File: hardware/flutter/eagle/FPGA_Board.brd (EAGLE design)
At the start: 100 x 77 mm, 38 parts, among them IC1 AT45DB161D-SU, U2 XC3S50AVQ100

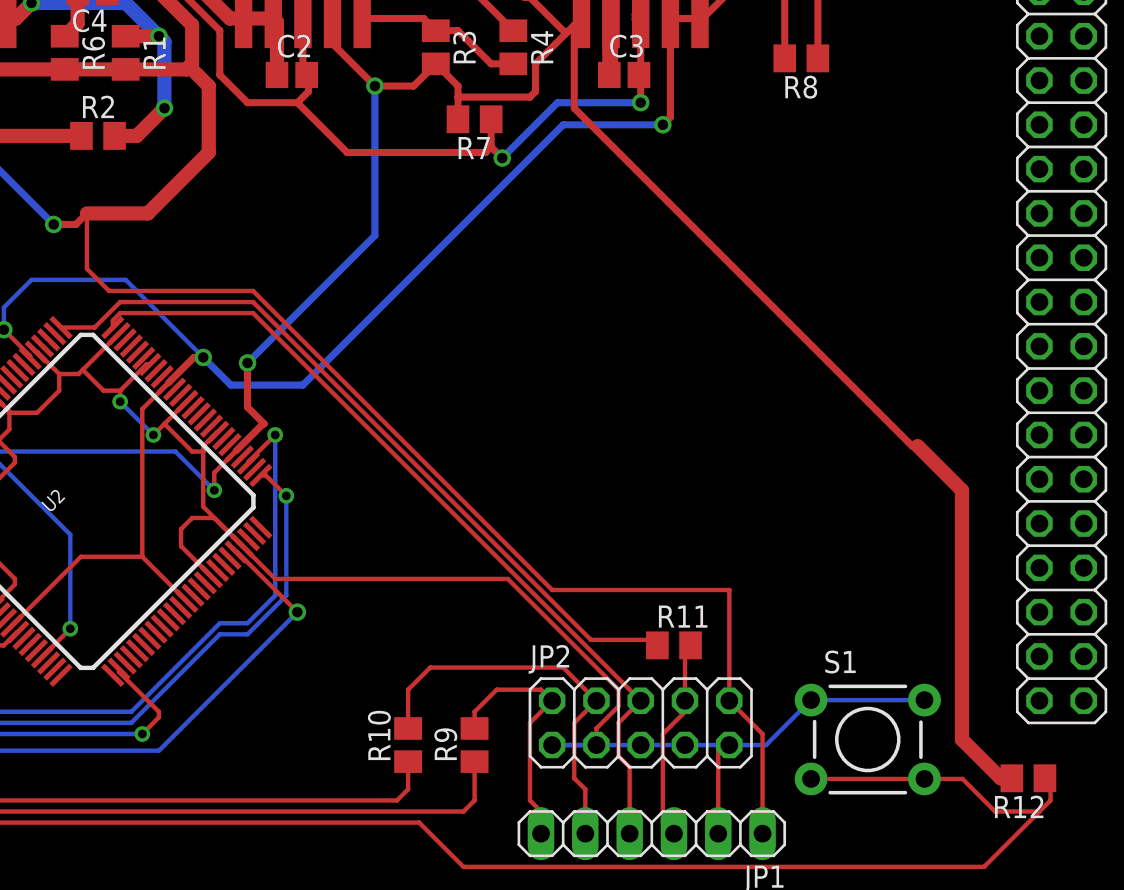
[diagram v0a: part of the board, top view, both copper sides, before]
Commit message: connected FPGA to friendship connector
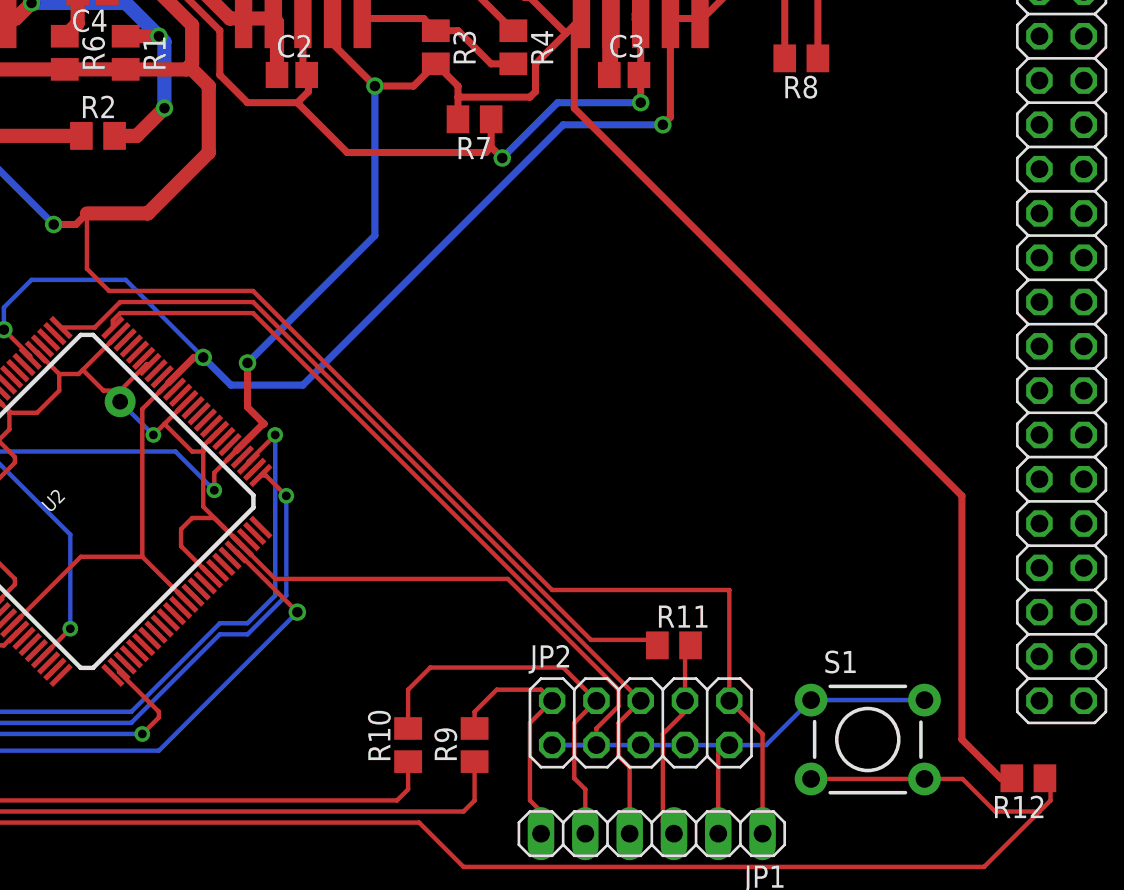
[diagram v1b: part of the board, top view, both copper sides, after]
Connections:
- new net FASTCLK+: U$4.A29(FASTCLK+)
- new net FASTCLK-: U$4.A28(FASTCLK-)
- new net FASTCLK/CLK: U$4.A27(GND), U2.P83, U2.P85
- new net FASTCLK/CS: U$4.A22(GND)
- new net FASTCLK/MOSI: U$4.A30(GND)
- new net FASTCLK3V3: U$4.A31(FASTCLK3V3)
- new net PPS: U$4.A26(PPS), U2.P89
- new net SLOWCLK/CLK: U$4.A24(SLOWCLKCLK), U2.P77
- new net SLOWCLK/CS: U$4.A25(SLOWCLK/CS), U2.P90
- new net SLOWCLK/MOSI: U$4.A23(SLOWTIMEMOSI), U2.P97
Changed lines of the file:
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@@
 <setting verticaltext="up"/>
 </settings>
-<grid distance="0.0125" unitdist="inch" unit="inch" style="lines" multiple="1" display="yes" altdistance="0.025" altunitdist="inch" altunit="inch"/>
+<grid distance="0.3175" unitdist="mm" unit="mm" style="lines" multiple="1" display="yes" altdistance="0.025" altunitdist="inch" altunit="inch"/>
 <layers>
 <layer number="1" name="Top" color="4" fill="1" visible="yes" active="yes"/>
@@
 <wire x1="42.773884375" y1="44.678884375" x2="41.275" y2="43.18" width="0.254" layer="1"/>
 <wire x1="41.275" y1="43.18" x2="41.275" y2="42.545" width="0.254" layer="1"/>
-<via x="41.275" y="42.545" extent="1-16" drill="0.5" shape="octagon"/>
+<via x="41.275" y="42.545" extent="1-16" drill="0.9" diameter="1.778" shape="octagon"/>
 <wire x1="41.275" y1="42.545" x2="43.18" y2="40.64" width="0.254" layer="16"/>
 <via x="43.18" y="40.64" extent="1-16" drill="0.5" shape="octagon"/>
@@
 <wire x1="46.6725" y1="37.465" x2="46.6725" y2="38.475646875" width="0.254" layer="1"/>
 <wire x1="46.6725" y1="38.475646875" x2="47.925990625" y2="39.7291375" width="0.254" layer="1"/>
-<wire x1="92.395" y1="20.955" x2="91.7575" y2="20.955" width="0.8128" layer="1"/>
-<wire x1="91.7575" y1="20.955" x2="89.535" y2="23.1775" width="0.8128" layer="1"/>
-<wire x1="89.535" y1="23.1775" x2="89.535" y2="37.465" width="0.8128" layer="1"/>
-<wire x1="89.535" y1="37.465" x2="86.995" y2="40.005" width="0.8128" layer="1"/>
-<wire x1="86.995" y1="40.005" x2="86.6775" y2="40.005" width="0.4064" layer="1"/>
-<wire x1="86.6775" y1="40.005" x2="67.31" y2="59.3725" width="0.4064" layer="1"/>
+<wire x1="92.395" y1="20.955" x2="91.7575" y2="20.955" width="0.4064" layer="1"/>
+<wire x1="91.7575" y1="20.955" x2="89.535" y2="23.1775" width="0.4064" layer="1"/>
+<wire x1="89.535" y1="23.1775" x2="89.535" y2="37.1475" width="0.4064" layer="1"/>
+<wire x1="89.535" y1="37.1475" x2="67.31" y2="59.3725" width="0.4064" layer="1"/>
 <wire x1="67.31" y1="59.3725" x2="67.31" y2="64.135" width="0.4064" layer="1"/>
 <wire x1="67.31" y1="64.135" x2="67.6275" y2="64.4525" width="0.4064" layer="1"/>
@@
 <contactref element="U2" pad="P54"/>
 </signal>
+<signal name="FASTCLK/CS">
+<contactref element="U$4" pad="A22(GND)"/>
+</signal>
+<signal name="SLOWCLK/MOSI">
+<contactref element="U$4" pad="A23(SLOWTIMEMOSI)"/>
+<contactref element="U2" pad="P97"/>
+<wire x1="30.460453125" y1="39.375584375" x2="69.5" y2="0.74" width="0" layer="19" extent="1-1"/>
+</signal>
+<signal name="SLOWCLK/CLK">
+<contactref element="U$4" pad="A24(SLOWCLKCLK)"/>
+<contactref element="U2" pad="P77"/>
+<wire x1="70.5" y1="0.74" x2="37.531521875" y2="46.44665" width="0" layer="19" extent="1-1"/>
+</signal>
+<signal name="SLOWCLK/CS">
+<contactref element="U$4" pad="A25(SLOWCLK/CS)"/>
+<contactref element="U2" pad="P90"/>
+<wire x1="32.935328125" y1="41.85045625" x2="71.5" y2="0.74" width="0" layer="19" extent="1-1"/>
+</signal>
+<signal name="PPS">
+<contactref element="U$4" pad="A26(PPS)"/>
+<contactref element="U2" pad="P89"/>
+<wire x1="72.5" y1="0.74" x2="33.28888125" y2="42.204009375" width="0" layer="19" extent="1-1"/>
+</signal>
+<signal name="FASTCLK/CLK">
+<contactref element="U$4" pad="A27(GND)"/>
+<contactref element="U2" pad="P83"/>
+<contactref element="U2" pad="P85"/>
+<wire x1="34.70309375" y1="43.618225" x2="35.4102" y2="44.32533125" width="0" layer="19" extent="1-1"/>
+<wire x1="73.5" y1="0.74" x2="34.70309375" y2="43.618225" width="0" layer="19" extent="1-1"/>
+</signal>
+<signal name="FASTCLK+">
+<contactref element="U$4" pad="A29(FASTCLK+)"/>
+</signal>
+<signal name="FASTCLK-">
+<contactref element="U$4" pad="A28(FASTCLK-)"/>
+</signal>
+<signal name="FASTCLK/MOSI">
+<contactref element="U$4" pad="A30(GND)"/>
+</signal>
+<signal name="FASTCLK3V3">
+<contactref element="U$4" pad="A31(FASTCLK3V3)"/>
+</signal>
 </signals>

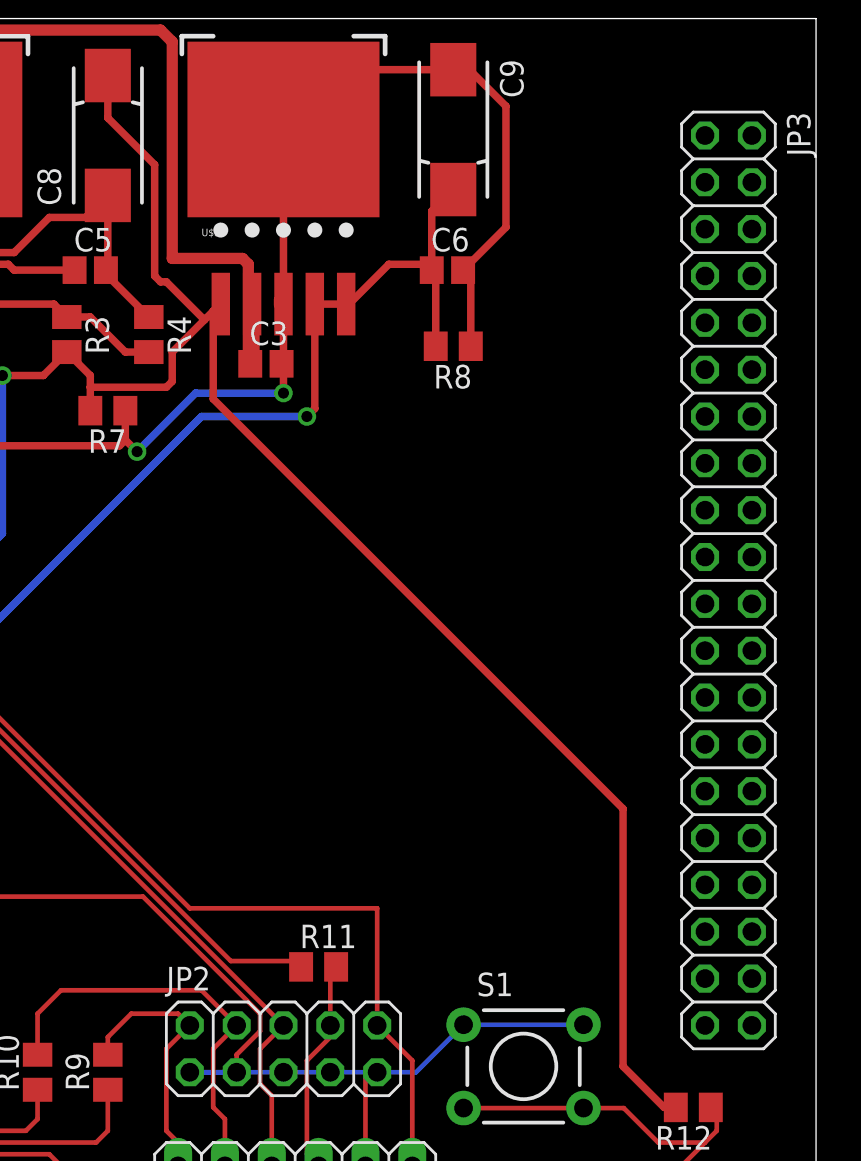
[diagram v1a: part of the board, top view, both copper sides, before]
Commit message: added atmega8 to flutter board
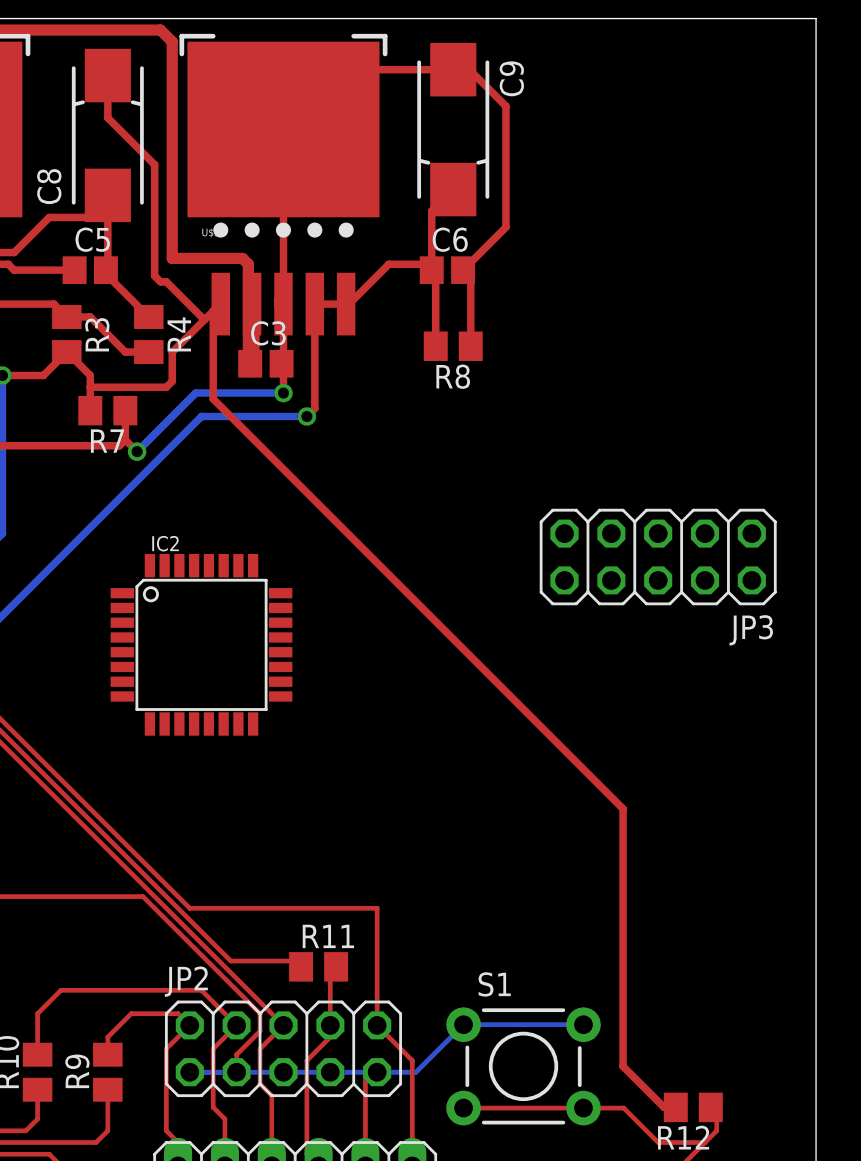
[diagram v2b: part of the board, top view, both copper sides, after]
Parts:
- added IC2: MEGA8-AI, atmel:TQFP32-08
- JP3: device pinhead:2X20 -> pinhead:2X05
- moved JP3 4.02 mm to (91.4, 50.8), turned to 180 degrees
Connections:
- removed net FASTCLK/CS: U$4.A22(GND)
- removed net FASTCLK/MOSI: U$4.A30(GND)
- new net AVCC: IC2.18
- net FASTCLK/CLK: no longer U$4.A27(GND)
- net GND: now also IC2.21, IC2.3, IC2.5, U$4.A07(GND), U$4.A09(GND), U$4.A11(GND), U$4.A22(GND), U$4.A27(GND), U$4.A30(GND)
- net VCC3.3: now also IC2.4, IC2.6
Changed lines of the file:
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@@
 <element name="R12" library="resistor" package="M0805" value="" x="93.345" y="20.955" rot="R180"/>
 <element name="S1" library="SparkFun" package="TACTILE-PTH" value="" x="84.1375" y="23.1775"/>
-<element name="JP3" library="pinhead" package="2X20" value="" x="95.25" y="49.53" rot="R270"/>
 <element name="U$4" library="hgg" package="FRIENDSHIP_EDGE_CONNECTOR" value="FRIENDSHIPCONNECTOR" x="0" y="15.24"/>
 <element name="IC1" library="atmel" package="8S2" value="AT45DB161D-SU" x="6.35" y="22.86">
@@
 <element name="R15" library="resistor" package="M0805" value="4.7K" x="3.4925" y="29.5275" rot="R90"/>
 <element name="U2" library="xilinx_devices" package="VQ100" value="XC3S50AVQ100" x="39.37" y="36.83" rot="R45"/>
+<element name="IC2" library="atmel" package="TQFP32-08" value="MEGA8-AI" x="66.675" y="46.0375">
+<attribute name="OC_NEWARK" value="73M8863" x="66.675" y="46.0375" size="1.778" layer="27" display="off"/>
+<attribute name="MPN" value="ATMEGA8-16AU" x="66.675" y="46.0375" size="1.778" layer="27" display="off"/>
+<attribute name="MF" value="" x="66.675" y="46.0375" size="1.778" layer="27" display="off"/>
+<attribute name="OC_FARNELL" value="9171371" x="66.675" y="46.0375" size="1.778" layer="27" display="off"/>
+</element>
+<element name="JP3" library="pinhead" package="2X05" value="" x="91.44" y="50.8" rot="R180"/>
 </elements>
 <signals>
@@
 <wire x1="80.3275" y1="77.2275" x2="74.3625" y2="77.2275" width="0.4064" layer="1"/>
 <wire x1="74.3625" y1="77.2275" x2="71.12" y2="73.985" width="0.4064" layer="1"/>
+<contactref element="IC2" pad="21"/>
+<contactref element="U$4" pad="A07(GND)"/>
+<contactref element="U$4" pad="A09(GND)"/>
+<contactref element="U$4" pad="A11(GND)"/>
+<contactref element="U$4" pad="A22(GND)"/>
+<contactref element="U$4" pad="A27(GND)"/>
+<contactref element="U$4" pad="A30(GND)"/>
+<contactref element="IC2" pad="5"/>
+<contactref element="IC2" pad="3"/>
 <wire x1="71.12" y1="64.4525" x2="71.12" y2="64.515" width="0" layer="19" extent="1-1"/>
 <wire x1="5.9575" y1="75.8825" x2="6.0325" y2="75.8825" width="0" layer="19" extent="1-1"/>
+<wire x1="62.3824" y1="47.2375" x2="63.1825" y2="56.515" width="0" layer="19" extent="1-16"/>
+<wire x1="62.3824" y1="45.6375" x2="62.3824" y2="47.2375" width="0" layer="19" extent="1-1"/>
+<wire x1="70.9676" y1="46.4375" x2="62.3824" y2="47.2375" width="0" layer="19" extent="1-1"/>
+<wire x1="76.5" y1="0.74" x2="75.565" y2="17.78" width="0" layer="19" extent="1-1"/>
+<wire x1="73.5" y1="0.74" x2="76.5" y2="0.74" width="0" layer="19" extent="1-1"/>
+<wire x1="68.5" y1="0.74" x2="73.5" y2="0.74" width="0" layer="19" extent="1-1"/>
+<wire x1="55.5" y1="0.74" x2="68.5" y2="0.74" width="0" layer="19" extent="1-1"/>
+<wire x1="53.5" y1="0.74" x2="55.5" y2="0.74" width="0" layer="19" extent="1-1"/>
+<wire x1="51.5" y1="0.74" x2="53.5" y2="0.74" width="0" layer="19" extent="1-1"/>
 </signal>
 <signal name="+5V">
@@
 <wire x1="37.465" y1="52.705" x2="38.735" y2="52.705" width="0.4064" layer="1"/>
 <wire x1="38.735" y1="52.705" x2="39.37" y2="53.34" width="0.4064" layer="1"/>
+<contactref element="IC2" pad="6"/>
+<contactref element="IC2" pad="4"/>
+<wire x1="62.3824" y1="44.8375" x2="62.3824" y2="46.4375" width="0" layer="19" extent="1-1"/>
+<wire x1="66.04" y1="31.75" x2="62.3824" y2="44.8375" width="0" layer="19" extent="1-1"/>
 </signal>
 <signal name="VCC2.5">
@@
 <contactref element="U2" pad="P54"/>
 </signal>
-<signal name="FASTCLK/CS">
-<contactref element="U$4" pad="A22(GND)"/>
-</signal>
 <signal name="SLOWCLK/MOSI">
 <contactref element="U$4" pad="A23(SLOWTIMEMOSI)"/>
@@
 </signal>
 <signal name="FASTCLK/CLK">
-<contactref element="U$4" pad="A27(GND)"/>
 <contactref element="U2" pad="P83"/>
 <contactref element="U2" pad="P85"/>
 <wire x1="34.70309375" y1="43.618225" x2="35.4102" y2="44.32533125" width="0" layer="19" extent="1-1"/>
-<wire x1="73.5" y1="0.74" x2="34.70309375" y2="43.618225" width="0" layer="19" extent="1-1"/>
 </signal>
 <signal name="FASTCLK+">
@@
 <contactref element="U$4" pad="A28(FASTCLK-)"/>
 </signal>
-<signal name="FASTCLK/MOSI">
-<contactref element="U$4" pad="A30(GND)"/>
-</signal>
 <signal name="FASTCLK3V3">
 <contactref element="U$4" pad="A31(FASTCLK3V3)"/>
 </signal>
+<signal name="AVCC">
+<contactref element="IC2" pad="18"/>
+</signal>
 </signals>

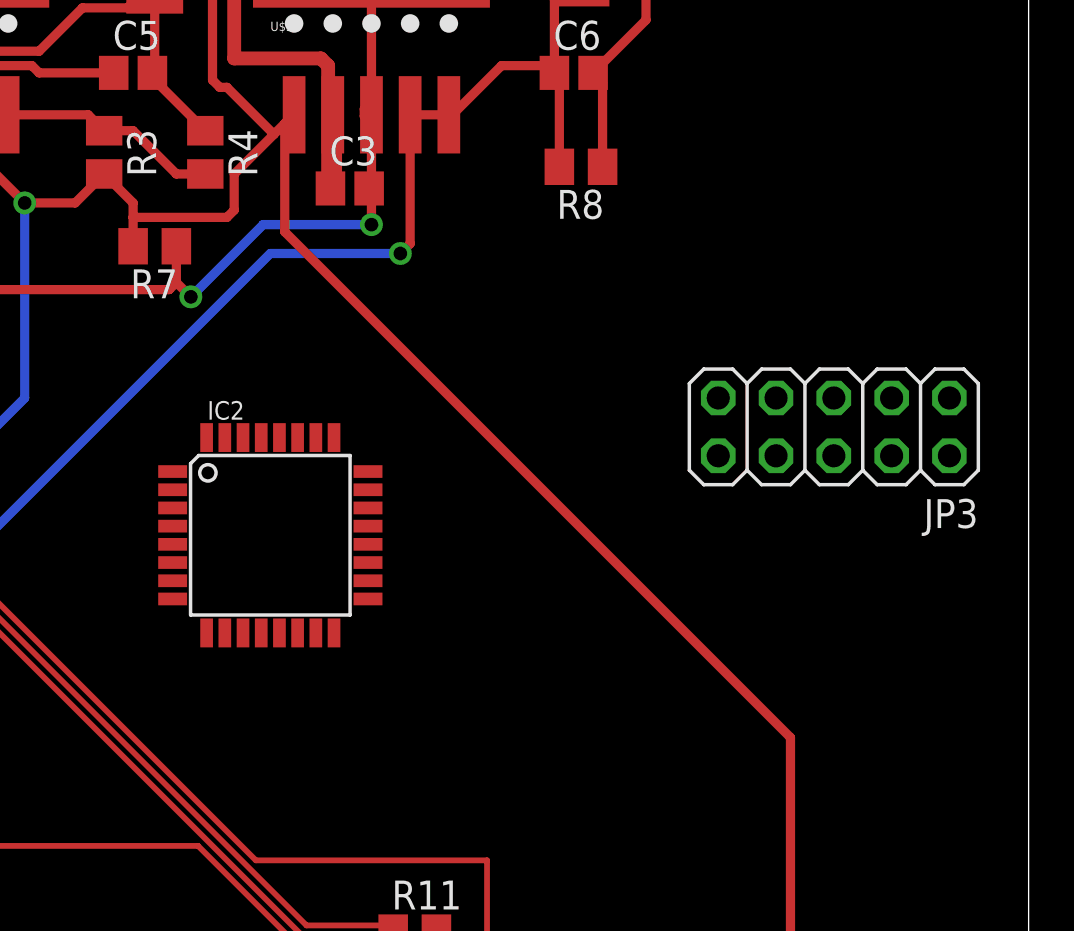
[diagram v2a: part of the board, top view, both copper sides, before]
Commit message: added RS485 level converter and 8MHz crystal to board (for uController)
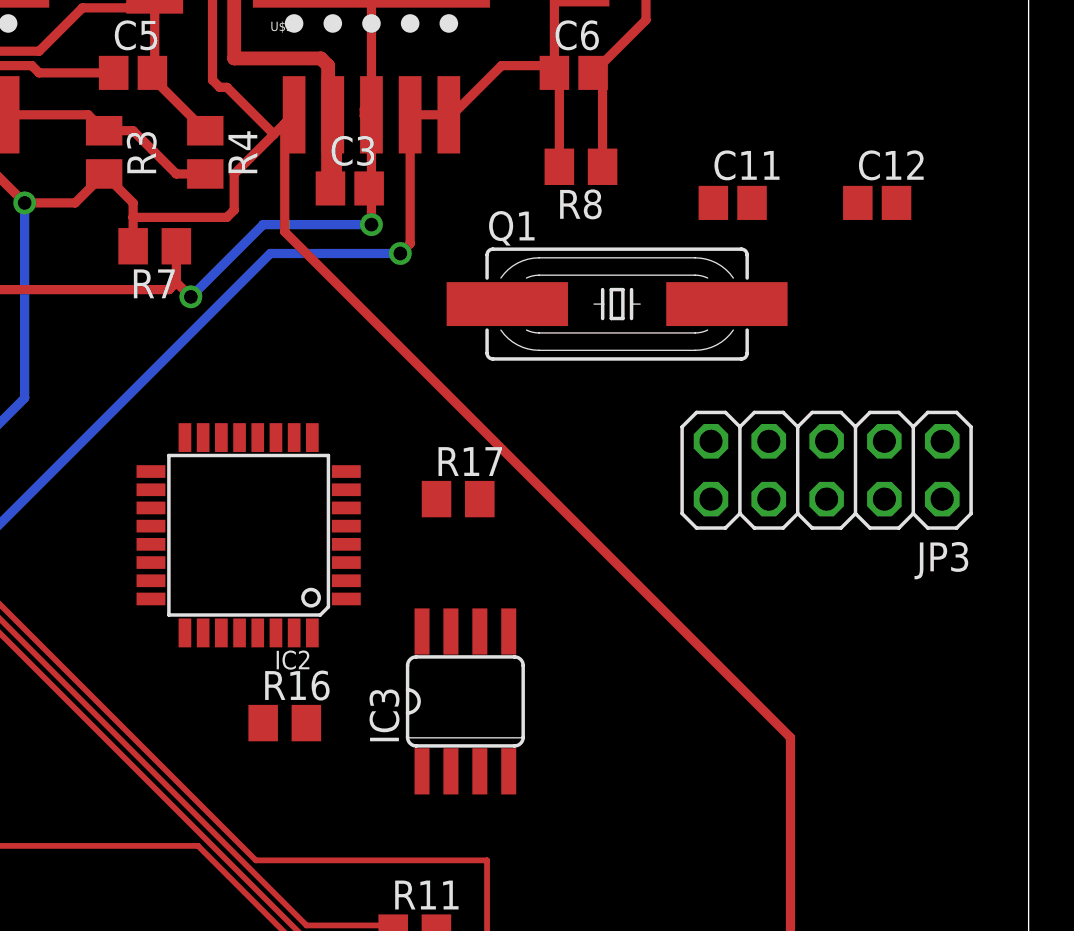
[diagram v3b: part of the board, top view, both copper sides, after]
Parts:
- added C11, C12: 22n, resistor:C0805
- added IC3: MAX3468CSA, maxim:SO08
- added Q1: 8Mhz, crystal:HC49UP
- added R16: 1k, resistor:M0805
- added R17: 1.6k, resistor:M0805
- JP1: value (none) -> JTAG2
- JP2: value (none) -> JTAG1
- JP3: value (none) -> ISP
- moved JP3 1.93 mm to (91.1, 48.9)
- moved IC2 0.95 mm to (65.7, 46.0), turned to 180 degrees
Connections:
- removed net FASTCLK/CLK: U2.P83, U2.P85
- new net N$10: IC3.6, R16.2
- new net N$11: C11.1, IC2.7, Q1.2
- new net N$12: C12.1, IC2.8, Q1.1
- new net N$5: IC3.8
- new net N$6: IC2.31, IC3.7
- new net N$9: IC2.30, R16.1, R17.2
- new net TRST: U$4.A16(TRST)
- new net UC_RX+: IC3.4, U$4.A18(TX+)
- new net UC_RX-: IC3.3, U$4.A17(TX-)
- new net UC_TX+: IC3.1, U$4.A20(RX+)
- new net UC_TX-: IC3.2, U$4.A21(RX-)
- net GND: now also C11.2, C12.2, IC3.5, R17.1, U$4.A19(GND)
- net SLOWCLK/CLK: no longer U2.P77
- net SLOWCLK/CS: no longer U2.P90
- net SLOWCLK/MOSI: no longer U2.P97
- net TCK: now also U$4.A15(TCK)
- net TDI: now also U$4.A12(TDI)
- net TDO: now also U$4.A13(TDO)
- net TMS: now also U$4.A14(TMS)
